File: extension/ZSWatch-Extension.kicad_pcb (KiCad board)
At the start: 4 copper layers, 16.8 x 16.8 mm, 40 parts, among them IC501 MAX32664, IC502 LIS2DS12, IC503 MAX86141, IC601 DA7212-01UM2, X701 MB2, X702 MB1, Y501 32kHz

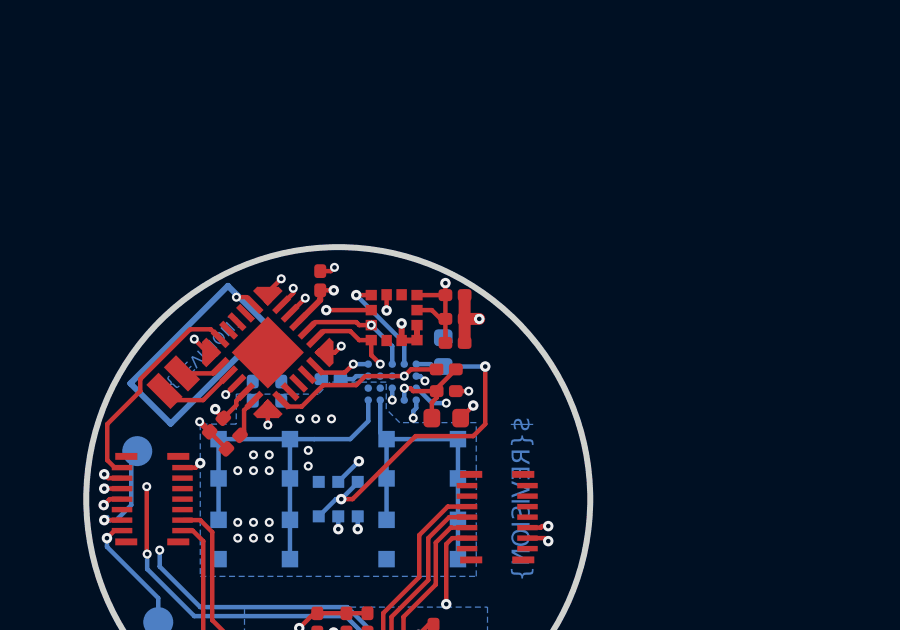
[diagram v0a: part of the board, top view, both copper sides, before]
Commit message: Bug: Issue #8, #9, #10
- Fix wrong silkscreen color and PCB color
- Remove silkscreen fragments
- Fix distance issues with capacitor pads and PCB outline

Closes: #8, #9, #10

Signed-off-by: Daniel Kampert <DanielKampert@kampis-elektroecke.de>
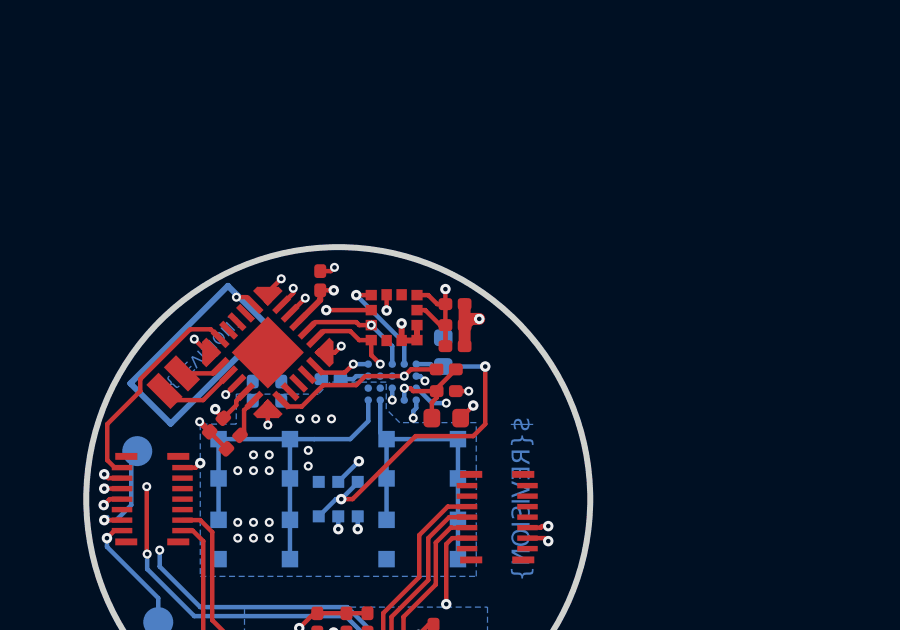
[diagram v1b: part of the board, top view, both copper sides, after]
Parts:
- moved C505 0.30 mm to (208.9, 143.5)
- moved C506 0.21 mm to (208.9, 144.2)
- moved C507 0.11 mm to (208.9, 144.9)
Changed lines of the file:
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@@
 			(layer "F.SilkS"
 				(type "Top Silk Screen")
-				(color "Black")
+				(color "White")
 			)
 			(layer "F.Paste"
@@
 			(layer "B.SilkS"
 				(type "Bottom Silk Screen")
-				(color "Black")
+				(color "White")
 			)
 			(copper_finish "HAL SnPb")
@@
 	(footprint "Capacitor_SMD:C_0201_0603Metric"
 		(layer "F.Cu")
-		(at 208.8925 143.2)
+		(at 208.8925 143.5)
 		(descr "Capacitor SMD 0201 (0603 Metric), square (rectangular) end terminal, IPC-7351 nominal, (Body size source: https://www.vishay.com/docs/20052/crcw0201e3.pdf), generated with kicad-footprint-generator")
 		(tags "capacitor")
@@
 	(footprint "Capacitor_SMD:C_0201_0603Metric"
 		(layer "F.Cu")
-		(at 208.8925 143.993)
+		(at 208.8925 144.2)
 		(descr "Capacitor SMD 0201 (0603 Metric), square (rectangular) end terminal, IPC-7351 nominal, (Body size source: https://www.vishay.com/docs/20052/crcw0201e3.pdf), generated with kicad-footprint-generator")
 		(tags "capacitor")
@@
 	(footprint "Capacitor_SMD:C_0201_0603Metric"
 		(layer "F.Cu")
-		(at 208.8925 144.793)
+		(at 208.8925 144.9)
 		(descr "Capacitor SMD 0201 (0603 Metric), square (rectangular) end terminal, IPC-7351 nominal, (Body size source: https://www.vishay.com/docs/20052/crcw0201e3.pdf), generated with kicad-footprint-generator")
 		(tags "capacitor")
@@
 		(attr smd)
 		(fp_line
-			(start -0.107836 -0.36)
-			(end 0.107836 -0.36)
-			(stroke
-				(width 0.12)
-				(type solid)
-			)
-			(layer "B.SilkS")
-		)
-		(fp_line
-			(start -0.107836 0.36)
-			(end 0.107836 0.36)
-			(stroke
-				(width 0.12)
-				(type solid)
-			)
-			(layer "B.SilkS")
-		)
-		(fp_line
 			(start 0.91 -0.46)
 			(end -0.91 -0.46)
@@
 			(keep_text_aligned yes)
 		)
-		(gr_text "16,8000 mm"
+		(gr_text "661,4173 mils"
 			(at 205 162.58 0)
 			(layer "User.6")
@@
 			(keep_text_aligned yes)
 		)
-		(gr_text "16,8000 mm"
+		(gr_text "661,4173 mils"
 			(at 218.08 150 90)
 			(layer "User.6")
@@
 	)
 	(segment
-		(start 209.2125 143.2)
-		(end 209.2125 143.993)
-		(width 0.4)
-		(layer "F.Cu")
-		(net 1)
-	)
-	(segment
 		(start 201.273726 148.314178)
 		(end 200.715561 147.756013)
@@
 	)
 	(segment
-		(start 209.2125 143.993)
-		(end 209.7 143.993)
-		(width 0.4)
-		(layer "F.Cu")
-		(net 1)
-	)
-	(segment
 		(start 200.379773 147.420227)
 		(end 200.71556 147.756014)
@@
 		(net 1)
 	)
-	(segment
-		(start 209.2125 143.993)
-		(end 209.2125 144.793)
-		(width 0.4)
-		(layer "F.Cu")
-		(net 1)
-	)
 	(via
 		(at 207.1125 144.143)
@@
 	)
 	(segment
-		(start 207.625 143.7)
-		(end 208.12 143.7)
-		(width 0.15)
-		(layer "F.Cu")
-		(net 69)
-	)
-	(segment
-		(start 208.572501 143.2)
-		(end 207.625 143.2)
-		(width 0.15)
-		(layer "F.Cu")
-		(net 69)
-	)
-	(segment
 		(start 197.54 151.05)
 		(end 197.7925 151.05)
@@
 	)
 	(segment
-		(start 208.5725 142.8)
-		(end 208.572501 142.800001)
-		(width 0.15)
-		(layer "F.Cu")
-		(net 69)
-	)
-	(segment
-		(start 208.5725 144.793001)
-		(end 208.5725 143.993)
-		(width 0.15)
-		(layer "F.Cu")
-		(net 69)
-	)
-	(segment
 		(start 208.28 146.315)
 		(end 208.92 145.675)
@@
 	)
 	(segment
-		(start 208.5725 143.993)
-		(end 208.572501 143.2)
-		(width 0.15)
-		(layer "F.Cu")
-		(net 69)
-	)
-	(segment
 		(start 207.202395 146.302417)
 		(end 207.402417 146.302417)
@@
 	)
 	(segment
-		(start 208.413 143.993)
-		(end 208.5725 143.993)
-		(width 0.15)
-		(layer "F.Cu")
-		(net 69)
-	)
-	(segment
 		(start 204.4 143.04)
 		(end 204.4 143.364469)
@@
 	)
 	(segment
-		(start 208.572501 142.800001)
-		(end 208.572501 143.2)
-		(width 0.15)
-		(layer "F.Cu")
-		(net 69)
-	)
-	(segment
-		(start 208.12 143.7)
-		(end 208.413 143.993)
-		(width 0.15)
-		(layer "F.Cu")
-		(net 69)
-	)
-	(segment
 		(start 200.9 147.035356)
 		(end 201.168109 147.303465)
@@
 	)
 	(via
-		(at 208.5725 142.8)
+		(at 208.572501 143)
 		(size 0.35)
 		(drill 0.15)
@@
 		)
 	)
+	(segment
+		(start 209.2125 143.5)
+		(end 209.2125 144.2)
+		(width 0.4)
+		(layer "F.Cu")
+		(net 1)
+	)
+	(segment
+		(start 209.2125 144.2)
+		(end 209.4195 143.993)
+		(width 0.4)
+		(layer "F.Cu")
+		(net 1)
+	)
+	(segment
+		(start 209.2125 144.2)
+		(end 209.2125 144.9)
+		(width 0.4)
+		(layer "F.Cu")
+		(net 1)
+	)
+	(segment
+		(start 209.4195 143.993)
+		(end 209.7 143.993)
+		(width 0.4)
+		(layer "F.Cu")
+		(net 1)
+	)
+	(segment
+		(start 208.5725 143.5)
+		(end 208.3 143.5)
+		(width 0.15)
+		(layer "F.Cu")
+		(net 69)
+	)
+	(segment
+		(start 207.625 143.7)
+		(end 207.9 143.7)
+		(width 0.15)
+		(layer "F.Cu")
+		(net 69)
+	)
+	(segment
+		(start 208.5725 143.5)
+		(end 208.5725 144.2)
+		(width 0.15)
+		(layer "F.Cu")
+		(net 69)
+	)
+	(segment
+		(start 208.5725 144.793001)
+		(end 208.5725 144.2)
+		(width 0.15)
+		(layer "F.Cu")
+		(net 69)
+	)
+	(segment
+		(start 208.572501 143.499999)
+		(end 208.5725 143.5)
+		(width 0.15)
+		(layer "F.Cu")
+		(net 69)
+	)
+	(segment
+		(start 208.3 143.5)
+		(end 208 143.2)
+		(width 0.15)
+		(layer "F.Cu")
+		(net 69)
+	)
+	(segment
+		(start 207.9 143.7)
+		(end 208.4 144.2)
+		(width 0.15)
+		(layer "F.Cu")
+		(net 69)
+	)
+	(segment
+		(start 208.572501 143)
+		(end 208.572501 143.499999)
+		(width 0.15)
+		(layer "F.Cu")
+		(net 69)
+	)
+	(segment
+		(start 208 143.2)
+		(end 207.625 143.2)
+		(width 0.15)
+		(layer "F.Cu")
+		(net 69)
+	)
+	(segment
+		(start 208.4 144.2)
+		(end 208.5725 144.2)
+		(width 0.15)
+		(layer "F.Cu")
+		(net 69)
+	)
 )
